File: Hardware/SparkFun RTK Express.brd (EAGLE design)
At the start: 68.2 x 110.1 mm, 182 parts, among them J13 Internal, J16 MICRO-SD-PUSH-PUSH-EXT-PIN, J17 Qwiic Right Angle, J3 USB Female Type C Connector, J4 External, J5 USB Female Type C Connector, Q1 SIL2308-TP, Q2 MBT3904DW1T1, U1 74HC4052D, U10 MCP73833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

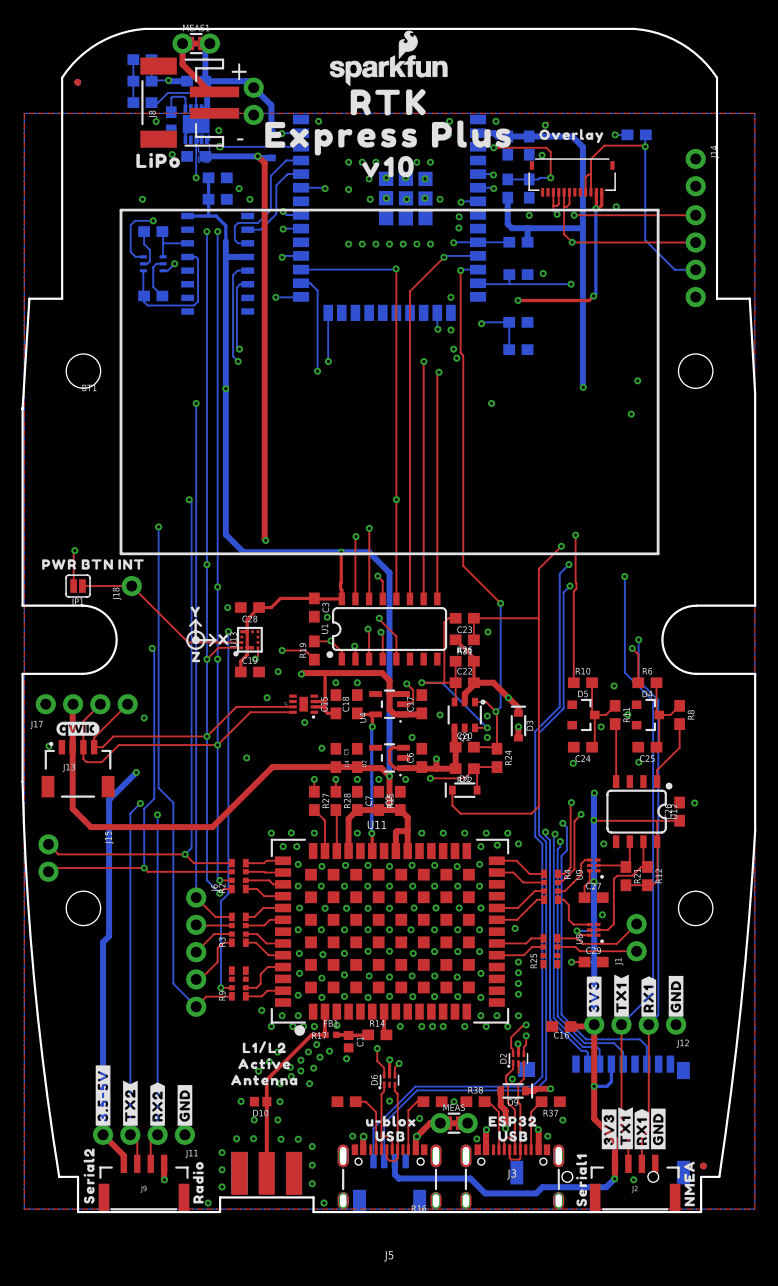
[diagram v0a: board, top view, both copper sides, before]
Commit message: Remove post mux opto isolation. Create v10 panel.
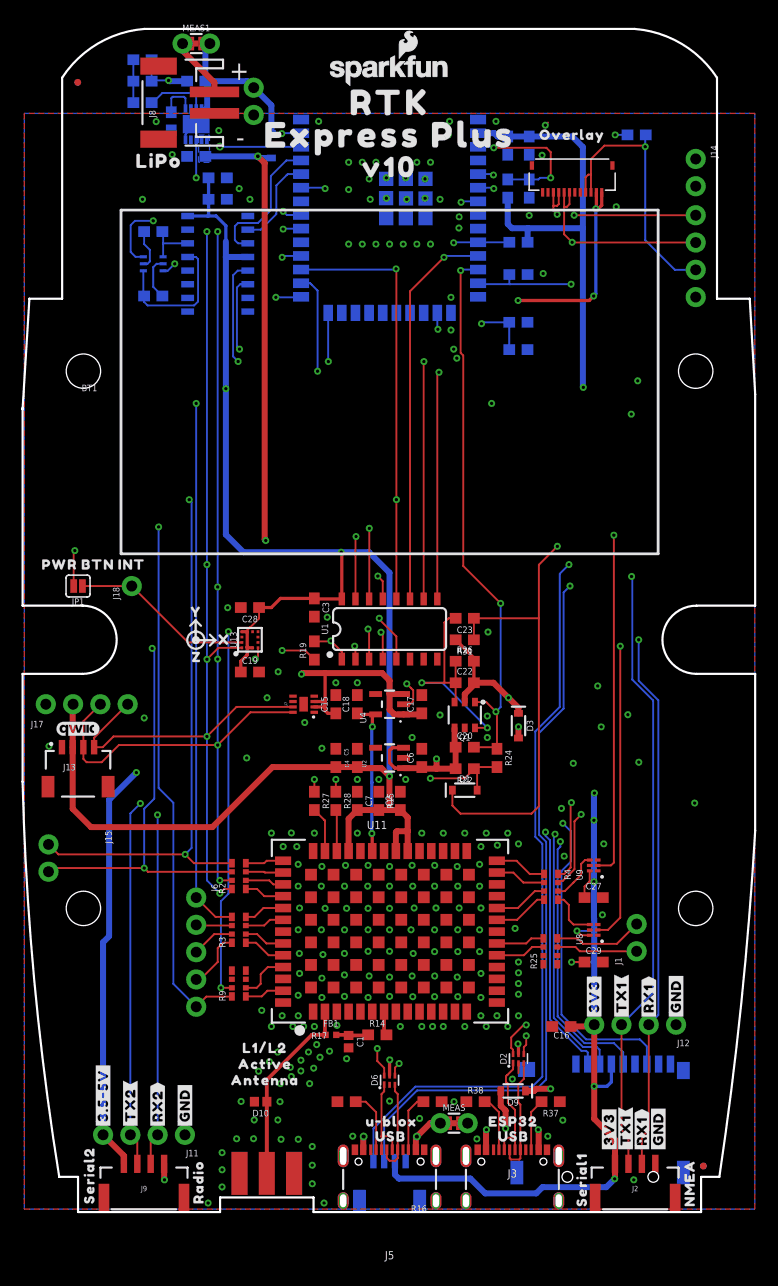
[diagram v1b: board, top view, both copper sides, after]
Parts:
- removed C24, C25: 1nF, SparkFun-Capacitors:0603
- removed C26: 0.1uF, SparkFun-Capacitors:0603
- removed D4, D5: BZX84C15LT3G, SparkFun-DiscreteSemi:SOT23-3
- removed R10, R6: 3.3k, SparkFun-Resistors:0603
- removed R11, R8: 470, SparkFun-Resistors:0603
- removed R12, R21: 910, SparkFun-Resistors:0603
- removed U12: HCPL-073L, SparkFun-DiscreteSemi:SO08
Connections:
- removed net DIR_IN: R11.2, U12.4
- removed net DIR_ISOLATED: R21.1, U12.6, U9.P2
- removed net N$35: C25.1, D4.3, R6.2, R8.1
- removed net N$37: C24.1, D5.3, R10.2, R11.1
- removed net WT_IN: R8.2, U12.1
- removed net WT_ISOLATED: R12.1, U12.7, U8.P2
- net 3.3V: no longer C26.1, R12.2, R21.2, U12.8
- net EXT_DIR: now also U9.P2; no longer R10.1
- net EXT_WT: now also U8.P2; no longer R6.1
- net GND: no longer C24.2, C25.2, C26.2, D4.1, D5.1, U12.2, U12.3, U12.5
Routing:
- net EXT_WT: track 30.6 -> 53.8 mm
- net EXT_DIR: track 40.2 -> 62.0 mm
- net 3.3V: track 343.4 -> 326.7 mm
- net WT_ISOLATED: track 12.0 -> 0.00 mm
- net N$37: track 8.46 -> 0.00 mm
- net N$35: track 8.46 -> 0.00 mm
- net WT_IN: track 6.22 -> 0.00 mm
- net DIR_IN: track 5.39 -> 0.00 mm
- net DIR_ISOLATED: track 5.18 -> 0.00 mm
- net GND: vias 205 -> 207
